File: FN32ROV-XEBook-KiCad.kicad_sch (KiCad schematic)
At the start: 0 parts

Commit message: Add IDC/JST/SD-breakout connector schematics
Places the five new connectors that replace the original FN32ROV SIO
plug/receptacle and onboard buttons/LEDs: a 12-pin right-angle IDC
header for the SIO signals, JST breakouts for the relocated LEDs and
buttons (net names matching XEBookButtonBar's existing swap/bt/rst
convention), a parallel SD-card breakout header, and a JST for the
power switch. ERC-clean; remaining warnings are expected single-use
nets that will resolve once the ESP32 and retained circuitry are wired
in.

Co-Authored-By: Claude Sonnet 5 <noreply@anthropic.com>
Claude-Session: https://claude.ai/code/session_01ATUvQCobb1cVELUyjLrcQZ
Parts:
- added J_BTN: BTN_JST, Connector_JST:JST_PH_S4B-PH-K_1x04_P2.00mm_Horizontal, symbol Connector_Generic:Conn_01x04
- added J_LED: LED_JST, Connector_JST:JST_PH_S4B-PH-K_1x04_P2.00mm_Horizontal, symbol Connector_Generic:Conn_01x04
- added J_PWR: PWR_SW_JST, Connector_JST:JST_PH_S2B-PH-K_1x02_P2.00mm_Horizontal, symbol Connector_Generic:Conn_01x02
- added J_SD: SD_BREAKOUT, Connector_PinHeader_2.54mm:PinHeader_1x07_P2.54mm_Vertical, symbol Connector_Generic:Conn_01x07
- added J_SIO: SIO_IDC, Connector_IDC:IDC-Header_2x06_P2.54mm_Latch_Horizontal, symbol Connector_Generic:Conn_02x06_Odd_Even
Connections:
- new net 3V3: J_LED.1 (Pin_1), J_SD.1 (Pin_1)
- new net BTN_BT: J_BTN.3 (Pin_3)
- new net BTN_RST: J_BTN.4 (Pin_4)
- new net BTN_SWAP: J_BTN.2 (Pin_2)
- new net GND: J_BTN.1 (Pin_1), J_SD.2 (Pin_2), J_SIO.4 (Pin_4)
- new net LED_BT: J_LED.3 (Pin_3)
- new net LED_SIO: J_LED.4 (Pin_4)
- new net LED_WIFI: J_LED.2 (Pin_2)
- new net PWR_SW_EN: J_PWR.2 (Pin_2)
- new net PWR_SW_VCC: J_PWR.1 (Pin_1)
- new net SD_CD: J_SD.7 (Pin_7)
- new net SD_CLK: J_SD.3 (Pin_3)
- new net SD_CS: J_SD.6 (Pin_6)
- new net SD_MISO: J_SD.5 (Pin_5)
- new net SD_MOSI: J_SD.4 (Pin_4)
- new net SIO_5V: J_SIO.9 (Pin_9)
- new net SIO_AUDIN: J_SIO.10 (Pin_10)
- new net SIO_CKIN: J_SIO.1 (Pin_1)
- new net SIO_CKOUT: J_SIO.2 (Pin_2)
- new net SIO_CMD: J_SIO.6 (Pin_6)
- new net SIO_DATAIN: J_SIO.3 (Pin_3)
- new net SIO_DATAOUT: J_SIO.5 (Pin_5)
- new net SIO_INT: J_SIO.11 (Pin_11)
- new net SIO_MCTL: J_SIO.7 (Pin_7)
- new net SIO_PROC: J_SIO.8 (Pin_8)
- no-connect marks 0 -> 1

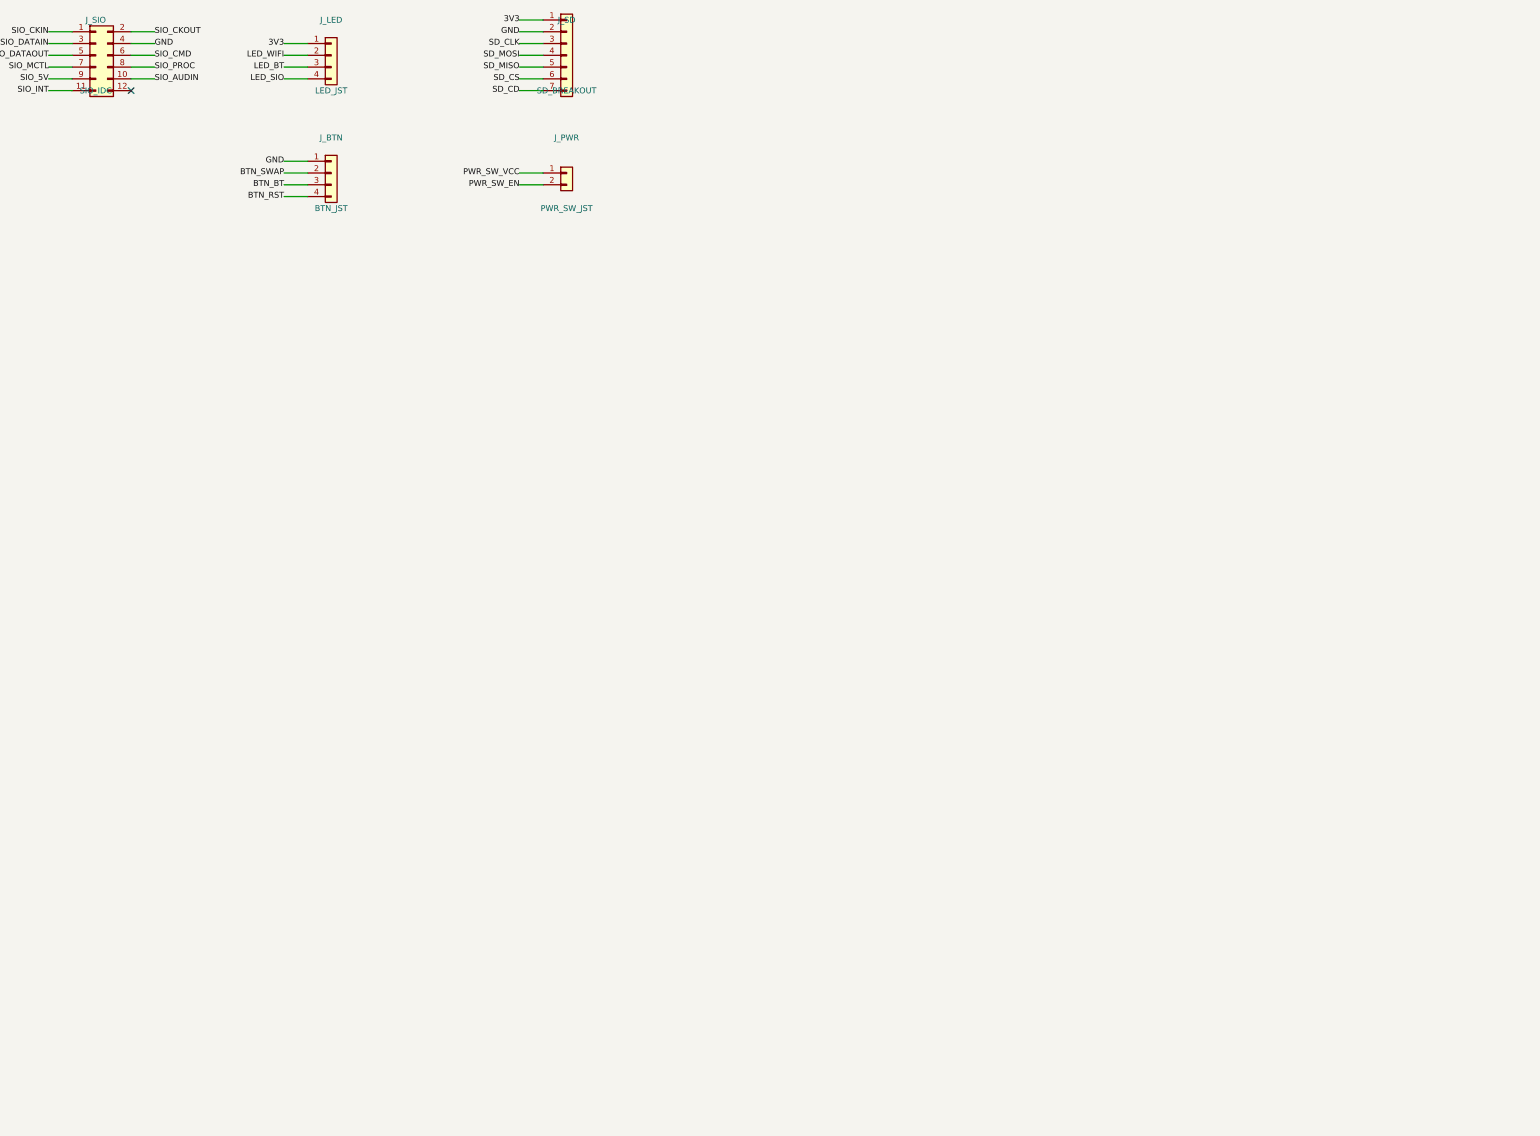
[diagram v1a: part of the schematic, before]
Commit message: Add ESP32-WROVER-E, SIO buffers, SD card, and sense/pullup network
Wires up the retained circuitry cross-checked pin-by-pin against the
original FN32ROV-1.7.1 schematic: the ESP32-WROVER-E module (real part
confirmed against the physical board, symbol/footprint sourced from
Espressif's official KiCad library v3.1.0 for KiCad-9 compatibility),
both SN74LS07 open-collector SIO buffers, the onboard microSD socket
wired in parallel with the SD breakout header, and the resistor/cap
network around the button-sense and pullup nodes.

ERC is down to 10 violations, all expected for this stage (nets
waiting on the not-yet-built USB-serial/reset circuit and power
regulator). Also adds project-level library tables for the Espressif
symbol/footprint, the one non-stock library this design needs.

Co-Authored-By: Claude Sonnet 5 <noreply@anthropic.com>
Claude-Session: https://claude.ai/code/session_01ATUvQCobb1cVELUyjLrcQZ
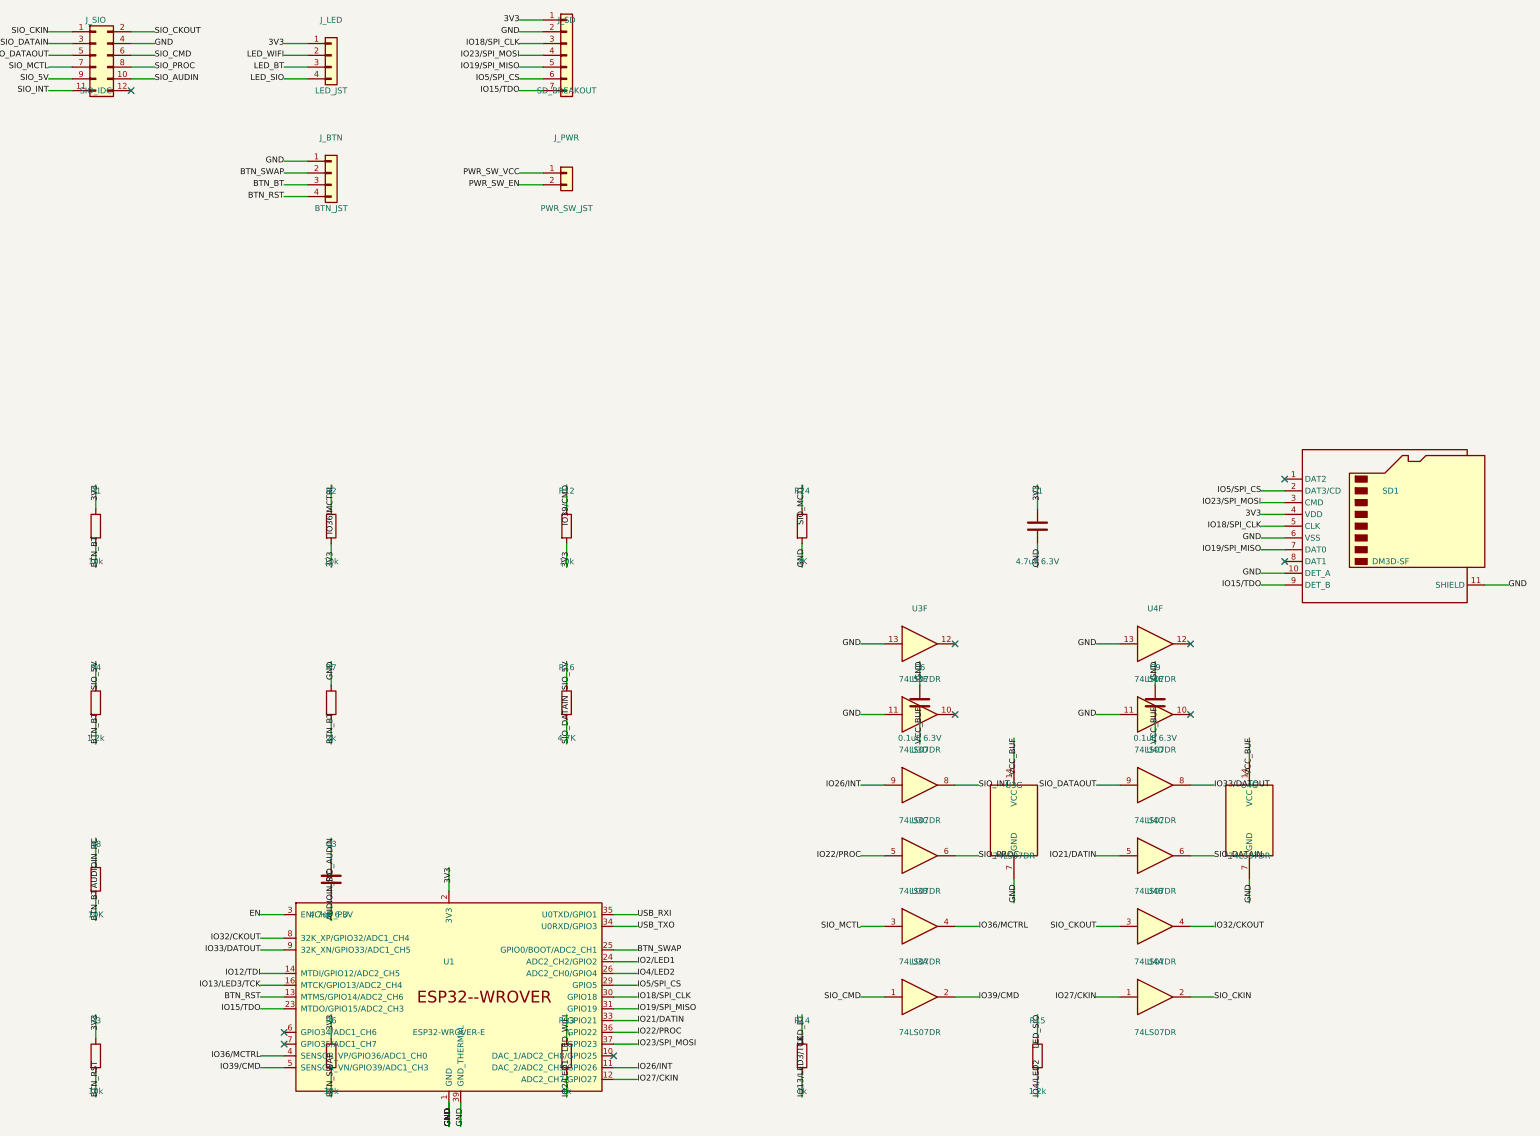
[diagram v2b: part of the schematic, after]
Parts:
- added C1, C3: 4.7uF 6.3V, Capacitor_SMD:C_0402_1005Metric, symbol Device:C
- added C6, C9: 0.1uF 6.3V, Capacitor_SMD:C_0402_1005Metric, symbol Device:C
- added R1, R12, R2, R3, R6: 10k, Resistor_SMD:R_0402_1005Metric, symbol Device:R
- added R13, R14: 1k, Resistor_SMD:R_0402_1005Metric, symbol Device:R
- added R15, R4: 1.2k, Resistor_SMD:R_0402_1005Metric, symbol Device:R
- added R16: 4.7K, Resistor_SMD:R_0402_1005Metric, symbol Device:R
- added R24: 2K, Resistor_SMD:R_0402_1005Metric, symbol Device:R
- added R7: 2k, Resistor_SMD:R_0402_1005Metric, symbol Device:R
- added R8: 10K, Resistor_SMD:R_0402_1005Metric, symbol Device:R
- added SD1: DM3D-SF, Connector_Card:microSD_HC_Hirose_DM3D-SF, symbol Connector:Micro_SD_Card_Det2
- added U1: ESP32-WROVER-E, Espressif:ESP32-WROVER-E, symbol Espressif:ESP32-WROVER-E
- added U3, U4: 74LS07DR, Package_SO:SOIC-14_3.9x8.7mm_P1.27mm, symbol 74xx:74LCX07
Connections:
- net 3V3: now also C1.1, R1.1, R12.2, R2.2, R3.1, R6.1, SD1.4 (VDD), U1.2 (3V3)
- net BTN_BT: now also R1.2, R4.2, R7.2, R8.2
- net BTN_RST: now also R3.2, U1.13 (MTMS/GPIO14/ADC2_CH6)
- net BTN_SWAP: now also R6.2, U1.25 (GPIO0/BOOT/ADC2_CH1)
- net GND: now also C1.2, C6.1, C9.1, R24.2, R7.1, SD1.10 (DET_A), SD1.11 (SHIELD), SD1.6 (VSS), U1.1 (GND), U1.15 (GND), U1.38 (GND), U1.39 (GND_THERMAL), U3.11, U3.13, U3.7 (GND), U4.11, U4.13, U4.7 (GND)
- net LED_BT: now also R14.1
- net LED_SIO: now also R15.1
- net LED_WIFI: now also R13.1
- net SIO_5V: now also R16.1, R4.1
- net SIO_AUDIN: now also C3.1
- net SIO_CKIN: now also U4.2
- net SIO_CKOUT: now also U4.3
- net SIO_CMD: now also U3.1
- net SIO_DATAIN: now also R16.2, U4.6
- net SIO_DATAOUT: now also U4.9
- net SIO_INT: now also U3.8
- net SIO_MCTL: now also R24.1, U3.3
- net SIO_PROC: now also U3.6
- net SD_CD renamed IO15/TDO
- net IO15/TDO: now also SD1.9 (DET_B), U1.23 (MTDO/GPIO15/ADC2_CH3)
- net SD_CLK renamed IO18/SPI_CLK
- net IO18/SPI_CLK: now also SD1.5 (CLK), U1.30 (GPIO18)
- net SD_CS renamed IO5/SPI_CS
- net IO5/SPI_CS: now also SD1.2 (DAT3/CD), U1.29 (GPIO5)
- net SD_MISO renamed IO19/SPI_MISO
- net IO19/SPI_MISO: now also SD1.7 (DAT0), U1.31 (GPIO19)
- net SD_MOSI renamed IO23/SPI_MOSI
- net IO23/SPI_MOSI: now also SD1.3 (CMD), U1.37 (GPIO23)
- new net AUDIOIN_RC: C3.2, R8.1
- new net EN: U1.3 (EN/CHIP_PU)
- new net IO12/TDI: U1.14 (MTDI/GPIO12/ADC2_CH5)
- new net IO13/LED3/TCK: R14.2, U1.16 (MTCK/GPIO13/ADC2_CH4)
- new net IO2/LED1: R13.2, U1.24 (ADC2_CH2/GPIO2)
- new net IO21/DATIN: U1.33 (GPIO21), U4.5
- new net IO22/PROC: U1.36 (GPIO22), U3.5
- new net IO26/INT: U1.11 (DAC_2/ADC2_CH9/GPIO26), U3.9
- new net IO27/CKIN: U1.12 (ADC2_CH7/GPIO27), U4.1
- new net IO32/CKOUT: U1.8 (32K_XP/GPIO32/ADC1_CH4), U4.4
- new net IO33/DATOUT: U1.9 (32K_XN/GPIO33/ADC1_CH5), U4.8
- new net IO36/MCTRL: R2.1, U1.4 (SENSOR_VP/GPIO36/ADC1_CH0), U3.4
- new net IO39/CMD: R12.1, U1.5 (SENSOR_VN/GPIO39/ADC1_CH3), U3.2
- new net IO4/LED2: R15.2, U1.26 (ADC2_CH0/GPIO4)
- new net USB_RXI: U1.35 (U0TXD/GPIO1)
- new net USB_TXO: U1.34 (U0RXD/GPIO3)
- new net VCC_BUF: C6.2, C9.2, U3.14 (VCC), U4.14 (VCC)
- no-connect marks 1 -> 10

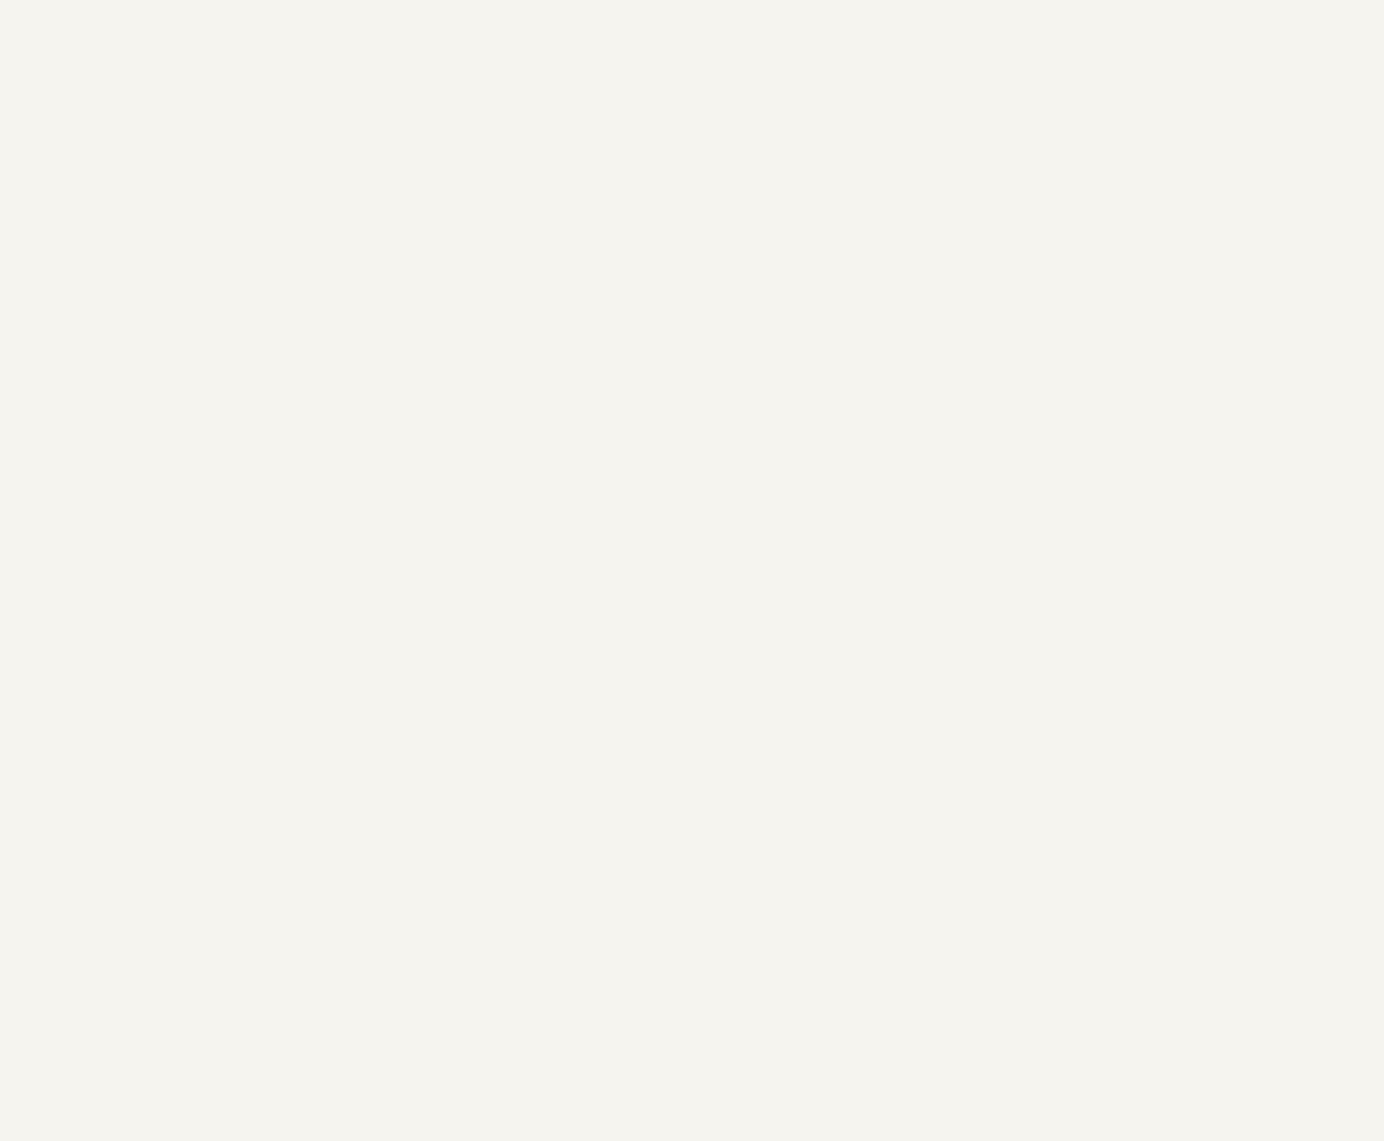
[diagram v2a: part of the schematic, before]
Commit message: Add CP2102N USB-serial, USB-C connector, and ESD protection
Wires up U2 (CP2102N-A02-GQFN24R), J2 (USB-C 16P using KiCad's stock
USB2.0 16P receptacle symbol, pins mapped by function since its A/B
pin naming differs from the original schematic's numbering), the three
ESD protection diodes on D+/D-/5V, and the supporting network: the
VBUS-sense divider (R9/R11) feeding the CP2102N's VBUS detect pin, the
RESET pullup (R10), and the CC2 pulldown (R25) — CC1 is intentionally
left unconnected, matching the original design.

U1's USB_RXI/USB_TXO nets are no longer dangling, confirming the
ESP32<->CP2102N UART link is correctly wired. ERC sits at 11 expected
violations, all waiting on the not-yet-built auto-reset transistor
circuit (Q1) or the power regulator.

Q1's exact internal pinout (which lead is base/collector/emitter on
the dual-transistor package) couldn't be determined with confidence
from the schematic image alone, so it's deliberately deferred rather
than guessed — RTS/DTR currently only reach U2, not yet Q1/EN/GPIO0.

Co-Authored-By: Claude Sonnet 5 <noreply@anthropic.com>
Claude-Session: https://claude.ai/code/session_01ATUvQCobb1cVELUyjLrcQZ
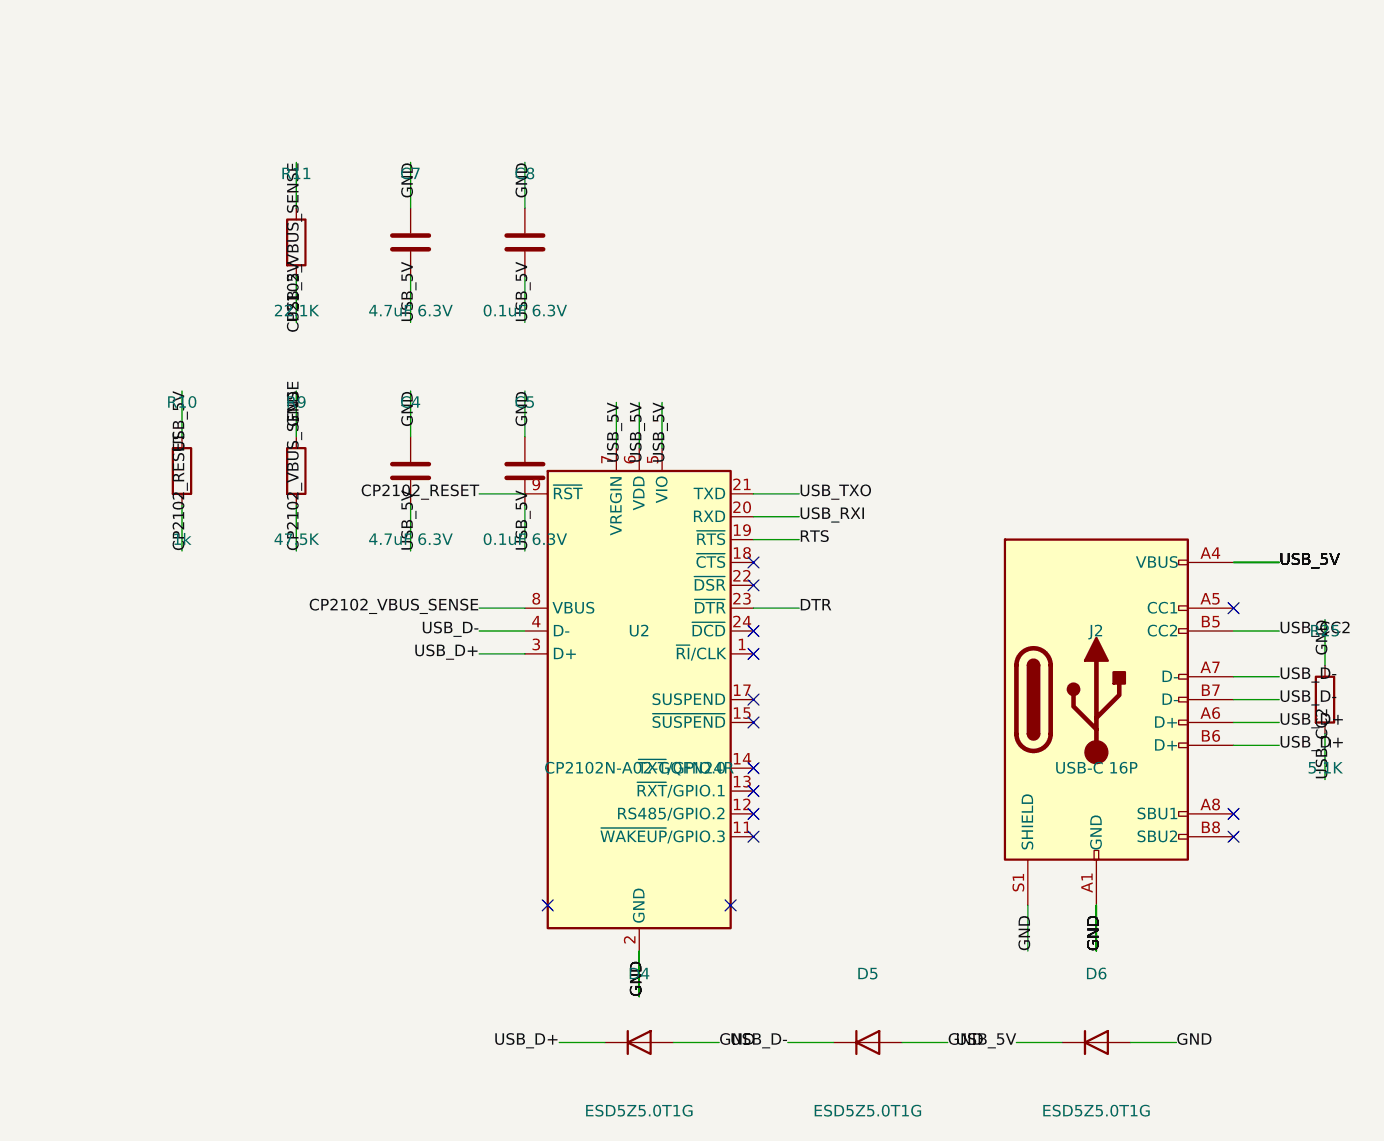
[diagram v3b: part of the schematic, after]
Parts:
- added C4, C7: 4.7uF 6.3V, Capacitor_SMD:C_0402_1005Metric, symbol Device:C
- added C5, C8: 0.1uF 6.3V, Capacitor_SMD:C_0402_1005Metric, symbol Device:C
- added D4, D5, D6: ESD5Z5.0T1G, Diode_SMD:D_SOD-523, symbol Device:D
- added J2: USB-C 16P, Connector_USB:USB_C_Receptacle_HCTL_HC-TYPE-C-16P-01A, symbol Connector:USB_C_Receptacle_USB2.0_16P
- added R10: 1k, Resistor_SMD:R_0402_1005Metric, symbol Device:R
- added R11: 22.1K, Resistor_SMD:R_0402_1005Metric, symbol Device:R
- added R25: 5.1K, Resistor_SMD:R_0402_1005Metric, symbol Device:R
- added R9: 47.5K, Resistor_SMD:R_0402_1005Metric, symbol Device:R
- added U2: CP2102N-A02-GQFN24R, Package_DFN_QFN:QFN-24-1EP_4x4mm_P0.5mm_EP2.6x2.6mm, symbol Interface_USB:CP2102N-Axx-xQFN24
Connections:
- net GND: now also C4.1, C5.1, C7.1, C8.1, D4.2 (A), D5.2 (A), D6.2 (A), J2.A1 (GND), J2.A12 (GND), J2.B1 (GND), J2.B12 (GND), J2.S1 (SHIELD), R25.1, R9.1, U2.2 (GND), U2.25 (GND)
- net USB_RXI: now also U2.20 (RXD)
- net USB_TXO: now also U2.21 (TXD)
- new net CP2102_RESET: R10.2, U2.9 (~{RST})
- new net CP2102_VBUS_SENSE: R11.1, R9.2, U2.8 (VBUS)
- new net DTR: U2.23 (~{DTR})
- new net RTS: U2.19 (~{RTS})
- new net USB_5V: C4.2, C5.2, C7.2, C8.2, D6.1 (K), J2.A4 (VBUS), J2.A9 (VBUS), J2.B4 (VBUS), J2.B9 (VBUS), R10.1, R11.2, U2.5 (VIO), U2.6 (VDD), U2.7 (VREGIN)
- new net USB_CC2: J2.B5 (CC2), R25.2
- new net USB_D+: D4.1 (K), J2.A6 (D+), J2.B6 (D+), U2.3 (D+)
- new net USB_D-: D5.1 (K), J2.A7 (D-), J2.B7 (D-), U2.4 (D-)
- no-connect marks 10 -> 25
